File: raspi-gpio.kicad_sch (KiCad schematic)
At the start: 3 parts, among them J88 Conn_01x20_RPi_GPIO_Odd, J89 Conn_02x20_Odd_Even, J90 Conn_01x20_RPi_GPIO_Even

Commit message: Add JLCPCB corrections
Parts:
- J88: JLCPCB_CORRECTION (none) -> 0;24.13;270
- J89: JLCPCB_CORRECTION (none) -> 1.27;24.13;270; now in the parts list
- J90: JLCPCB_CORRECTION (none) -> 2.54;24.13;270
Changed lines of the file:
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@@
+			"AAAAAAAAAAAAAAAAAAAAAAAAAAAAAAAAAAAAAAAAAAAAAAAAAAAAAAAAAAAAAAAAAAAAAAAAAAAA"
+			"AAAAAAAAAAAAAAAAAAAAAAAAAAAAAAAAAAAAAAAAAAAAAAAAAAAAAAAAAAAAAAAAAAAAAAAAAAAA"
+			"AAAAAAAAAAAAAAAAAAAAAAAAAAAAAAAAAAAAAAAAAAAAAAAAAAAAAAAAAAAAAAAAAAAAAAAAAAAA"
+			"AAAAAAAAAAAAAAAAAAAAAAAAAAAAAAAAAAAAAAAAAAAAAAAAAAAAAAAAAAAAAAAAAAAAAAAAAAAA"
+			"AAAAAAAAAAAAAAAAAAAAAAAAAAAAAAAAAAAAAAAAAAAAAAAAAAAAAAAAAAAAAAAAAAAAAAAAAAAA"
+			"AAAAAAAAAAAAAAAAAAAAAAAAAAAAAAAAAAAAAAAAAAAAAAAAAAAAAAAAAAAAAAAAAAAAAAAAAAAA"
+			"AAAAAAAAAAAAAAAAAAAAAAAAAAAAAAAAAAAAAAAAAAAAAAAAAAAAAAAAAAAAAAAAAAAAAAAAAAAA"
+			"AAAAAAAAAAAAAAAAAAAAAAAAAAAAAAAAAAAAAAAAAAAAAAAAAAAAAAAAAAAAAAAAAAAAAAAAAAAA"
+			"AAAAAAAAAAAAAAAAAAAAAAAAAAAAAAAAAAAAAAAAAAAAAAAAAAAAAAAAAAAAAAAAAAAAAAAAAAAA"
+			"AAAAAAAAAAAAAAAAAAAAAAAAAAAAAAAAAAAAAAAAAAAAAAAAAAAAAAAAAAAAAAAAAAAAAAAAAAAA"
+			"AAAAAAAAAAAAAAAAAAAAAAAAAAAAAAAAAAAAAAAAAAAAAAAAAAAAAAAAAAAAAAAAAAAAAAAAAAAA"
+			"AAAAAAAAAAAAAAAAAAAAAAAAAAAAAAAAAAAAAAAAAAAAAAAAAAAAAAAAAAAAAAAAAAAAAAAAAAAA"
+			"AAAAAAAAAAAAAAAAAAAAAAAAAAAAAAAAAAAAAAAAAAAAAAAAAAAAAAAAAAAAAAAAAAAAAAAAAAAA"
+			"AAAAAAAAAAAAAAAAAAAAAAAAAAAAAAAAAAAAAAAAAAAAAAAAAAAAAAAAAAAAAAAAAAAAAAAAAAAA"
+			"AAAAAAAAAAAAAAAAAAAAAAAAAAAAAAAAAAAAAAAAAAAAAAAAAAAAAAAAAAAAAAAAAAAAAAAAAAAA"
+			"AAAAAAAAAAAAAAAAAAAAAAAAAAAAAAAAAAAAAAAAAAAAAAAAAAAAAAAAAAAAAAAAAAAAAAAAAAAA"
+			"AAAAAAAAAAAAAAAAAAAAAAAAAAAAAAAAAAAAAAAAAAAAAAAAAAAAAAAAAAAAAAAAAAAAAAAAAAAA"
+			"AAAAAAAAAAAAAAAAAAAAAAAAAAAAAAAAAAAAAAAAAAAAAAAAAAAAAAAAAAAAAAAAAAAAAAAAAAAA"
+			"AAAAAAAAAAAAAAAAAAAAAAAAAAAAAAAAAAAAAAAAAAAAAAAAAAAAAAAAAAAAAAAAAAAAAAAAAAAA"
+			"AAAAAAAAAAAAAAAAAAAAAAAAAAAAAAAAAAAAAAAAAAAAAAAAAAAAAAAAAAAAAAAAAAAAAAAAAAAA"
+			"AAAAAAAAAAAAAAAAAAAAAAAAAAAAAAAAAAAAAAAAAAAAAAAAAAAAAAAAAAAAAAAAAAAAAAAAAAAA"
+			"AAAAAAAAAAAAAAAAAAAAAAAAAAAAAAAAAAAAAAAAAAAAAAAAAAAAAAAAAAAAAAAAAAAAAAAAAAAA"
+			"AAAAAAAAAAAAAAAAAAAAAAAAAAAAAAAAAAAAAAAAAAAAAAAAAAAAAAAAAAAAAAAAAAAAAAAAAAAA"
+			"AAAAAAAAAAAAAAAAAAAAAAAAAAAAAAAAAAAAAAAAAAAAAAAAAAAAAAAAAAAAAAAAAAAAAAAAAAAA"
+			"AAAAAAAAAAAAAAAAAAAAAAAAAAAAAAAAAAAAAAAAAAAAAAAAAAAAAAAAAAAAAAAAAAAAAAAAAAAA"
+			"AAAAAAAAAAAAAAAAAAAAAAAAAAAAAAAAAAAAAAAAAAAAAAAAAAAAAAAAAAAAAAAAAAAAAAAAAAAA"
+			"AAAAAAAAAAAAAAAAAAAAAAAAAAAAAAAAAAAAAAAAAAAAAAAAAAAAAAAAAAAAAAAAAAAAAAAAAAAA"
+			"AAAAAAAAAAAAAAAAAAAAAAAAAAAAAAAAAAAAAAAAAAAAAAAAAAAAAAAAAAAAAAAAAAAAAAAAAAAA"
+			"AAAAAAAAAAAAAAAAAAAAAAAAAAAAAAAAAAAAAAAAAAAAAAAAAAAAAAAAAAAAAAAAAAAAAAAAAAAA"
+			"AAAAAAAAAAAAAAAAAAAAAAAAAAAAAAAAAAAAAAAAAAAAAAAAAAAAAAAAAAAAAAAAAAAAAAAAAAAA"
+			"AAAAAAAAAAAAAAAAAAAAAAAAAAAAAAAAAAAAAAAAAAAAAAAAAAAAAAAAAAAAAAAAAAAAAAAAAAAA"
+			"AAAAAAAAAAAAAAAAAAAAAAAAAAAAAAAAAAAAAAAAAAAAAAAAAAAAAAAAAAAAAAAAAAAAAAAAAAAA"
+			"AAAAAAAAAAAAAAAAAAAAAAAAAAAAAAAAAAAAAAAAAAAAAAAAAAAAAAAAAAAAAAAAAAAAAAAAAAAA"
+			"AAAAAAAAAAAAAAAAAAAAAAAAAAAAAAAAAAAAAAAAAAAAAAAAAAAAAAAAAAAAAAAAAAAAAAAAAAAA"
+			"AAAAAAAAAAAAAAAAAAAAAAAAAAAAAAAAAAAAAAAAAAAAAAAAAAAAAAAAAAAAAAAAAAAAAAAAAAAA"
+			"AAAAAAAAAAAAAAAAAAAAAAAAAAAAAAAAAAAAAAAAAAAAAAAAAAAAAAAAAAAAAAAAAAAAAAAAAAAA"
 			"AAAAAAAAAAAAAAAAAAAAAAAAAAAAAAAAAAAAAAAAAAAAAAAAAAAAAAAAAAAAAAAAAAAAAAAAAAAA"
 			"AAAAAAAAAAAAAAAAAAAAAAAAAAAAAAAAAAAAAAAAAAAAAAAAAAAAAAAAAAAAAAAAAAAAAAAAAAAA"
@@
 			)
 		)
+		(property "JLCPCB_CORRECTION" "0;24.13;270"
+			(at 119.38 83.82 0)
+			(effects
+				(font
+					(size 1.27 1.27)
+				)
+				(hide yes)
+			)
+		)
 		(pin "35"
 		)
@@
 		(unit 1)
 		(exclude_from_sim no)
-		(in_bom no)
+		(in_bom yes)
 		(on_board yes)
 		(dnp no)
@@
 		)
 		(property "THT_LCSC" ""
+			(at 142.24 83.82 0)
+			(effects
+				(font
+					(size 1.27 1.27)
+				)
+				(hide yes)
+			)
+		)
+		(property "JLCPCB_CORRECTION" "1.27;24.13;270"
 			(at 142.24 83.82 0)
 			(effects
@@
 			(at 167.64 83.82 0)
 			(effects
+				(font
+					(size 1.27 1.27)
+				)
+				(hide yes)
+			)
+		)
+		(property "JLCPCB_CORRECTION" "2.54;24.13;270"
+			(at 167.64 83.82 0)
+			(effects

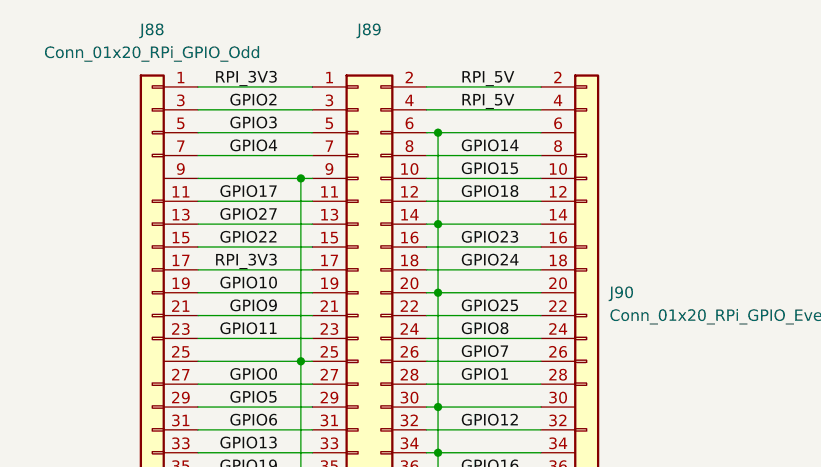
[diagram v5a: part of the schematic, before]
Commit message: Improve MCU2 layout; document curlim12v CSA
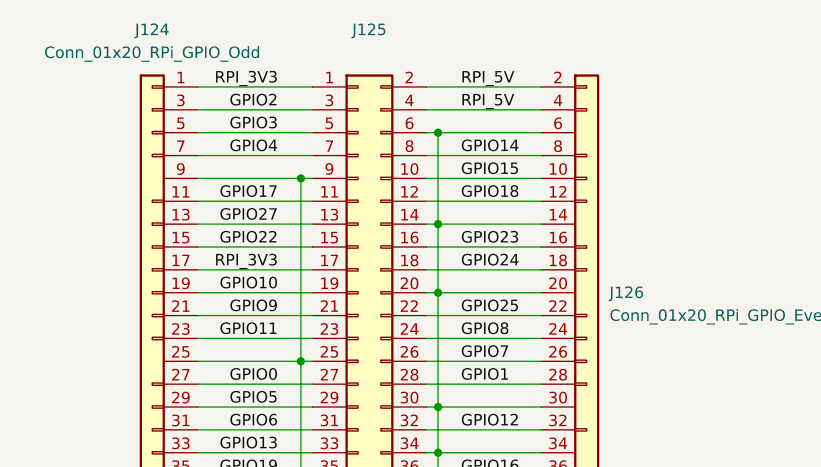
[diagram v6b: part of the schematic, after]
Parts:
- renumbered J88 to J124, J89 to J125, J90 to J126
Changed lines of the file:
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@@
 		(dnp no)
 		(fields_autoplaced yes)
-		(property "Reference" "J88"
+		(property "Reference" "J124"
 			(at 119.38 54.61 0)
 			(effects
@@
 			(project ""
 				(path "/7eeba806-440e-4671-bc07-69fe183910a7/d60c1020-d2cb-4d48-a4f2-2128439747bd"
-					(reference "J88")
+					(reference "J124")
 					(unit 1)
 				)
@@
 		(dnp no)
 		(fields_autoplaced yes)
-		(property "Reference" "J89"
+		(property "Reference" "J125"
 			(at 143.51 54.61 0)
 			(effects
@@
 			(project ""
 				(path "/7eeba806-440e-4671-bc07-69fe183910a7/d60c1020-d2cb-4d48-a4f2-2128439747bd"
-					(reference "J89")
+					(reference "J125")
 					(unit 1)
 				)
@@
 		(dnp no)
 		(fields_autoplaced yes)
-		(property "Reference" "J90"
+		(property "Reference" "J126"
 			(at 170.18 83.8199 0)
 			(effects
@@
 			(project ""
 				(path "/7eeba806-440e-4671-bc07-69fe183910a7/d60c1020-d2cb-4d48-a4f2-2128439747bd"
-					(reference "J90")
+					(reference "J126")
 					(unit 1)
 				)
@@
 		(dnp no)
 		(fields_autoplaced yes)
-		(property "Reference" "#PWR0270"
+		(property "Reference" "#PWR0271"
 			(at 135.89 118.11 0)
 			(effects
@@
 			(project ""
 				(path "/7eeba806-440e-4671-bc07-69fe183910a7/d60c1020-d2cb-4d48-a4f2-2128439747bd"
-					(reference "#PWR0270")
+					(reference "#PWR0271")
 					(unit 1)
 				)
@@
 		(dnp no)
 		(fields_autoplaced yes)
-		(property "Reference" "#PWR0271"
+		(property "Reference" "#PWR0272"
 			(at 151.13 118.11 0)
 			(effects
@@
 			(project "HALSPA"
 				(path "/7eeba806-440e-4671-bc07-69fe183910a7/d60c1020-d2cb-4d48-a4f2-2128439747bd"
-					(reference "#PWR0271")
+					(reference "#PWR0272")
 					(unit 1)
 				)

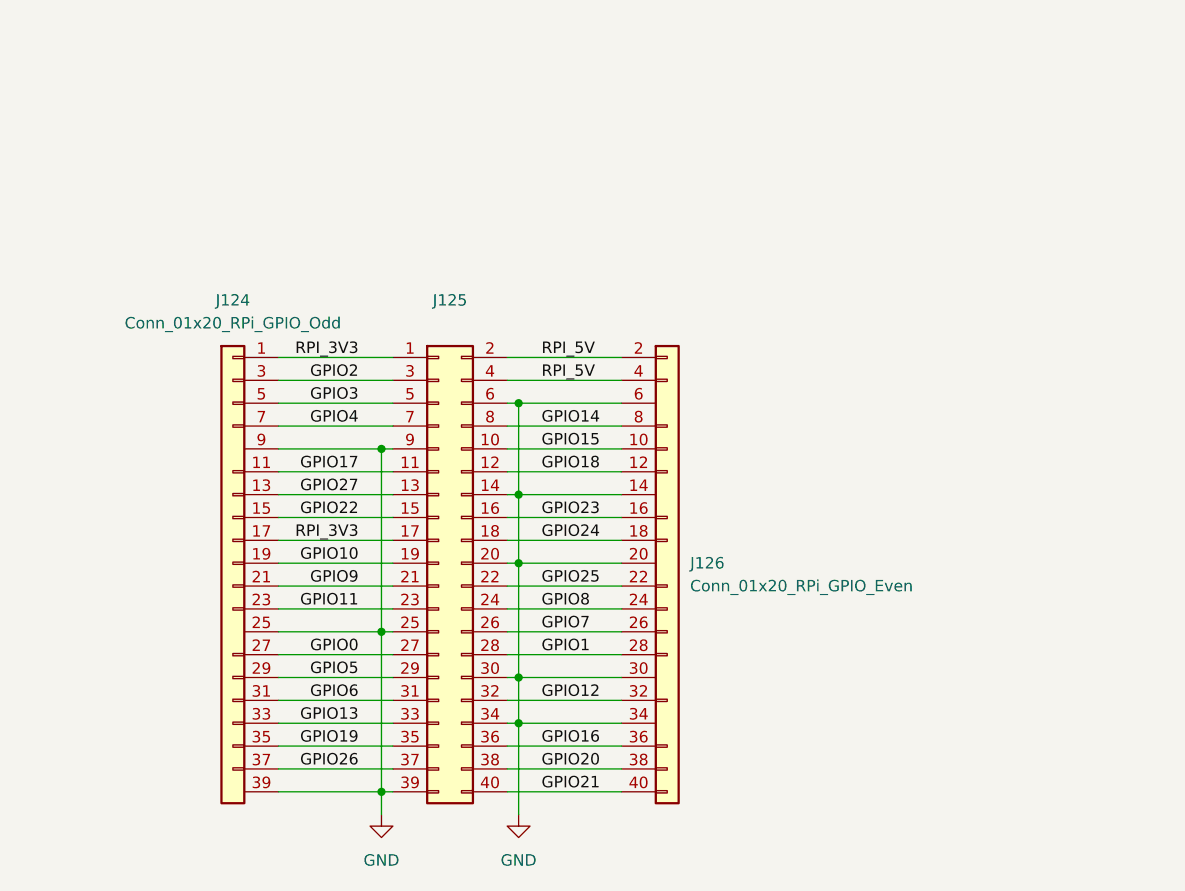
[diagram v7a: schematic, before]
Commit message: Update the design to a stackable one
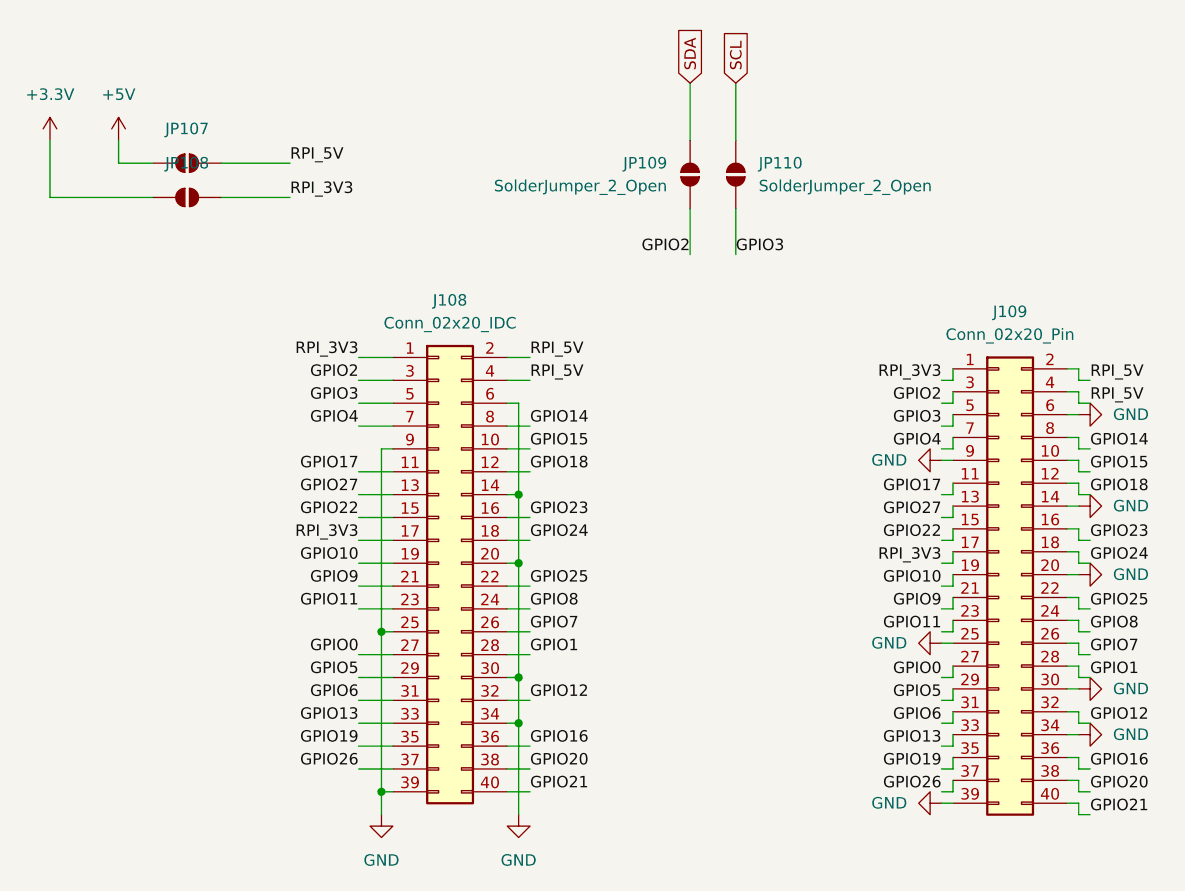
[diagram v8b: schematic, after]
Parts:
- removed J124: Conn_01x20_RPi_GPIO_Odd, HL_Connector_Pad_2.54mm:Pad_2x20_P2.54_1.7x1.7_RPi_GPIO_Odd, symbol HL_Connector_Pad_2.54mm:Conn_01x20_RPi_GPIO_Odd
- removed J126: Conn_01x20_RPi_GPIO_Even, HL_Connector_Pad_2.54mm:Pad_2x20_P2.54_1.7x1.7_RPi_GPIO_Even, symbol HL_Connector_Pad_2.54mm:Conn_01x20_RPi_GPIO_Even
- added J109: Conn_02x20_Pin, HL_Connector_Pad_2.54mm:Pad_2x20_P2.54_1.7x1.7_RPi-GPIO, symbol Connector_Generic:Conn_02x20_Odd_Even
- added JP107, JP108, JP109, JP110: SolderJumper_2_Open, Jumper:SolderJumper-2_P1.3mm_Open_TrianglePad1.0x1.5mm, symbol Jumper:SolderJumper_2_Open
- J108: renamed from J125; value Conn_02x20_Odd_Even -> Conn_02x20_IDC
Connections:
- net GND: now also J109.14 (Pin_14), J109.20 (Pin_20), J109.25 (Pin_25), J109.30 (Pin_30), J109.34 (Pin_34), J109.39 (Pin_39), J109.6 (Pin_6), J109.9 (Pin_9)
- net GPIO0: now also J109.27 (Pin_27)
- net GPIO1: now also J109.28 (Pin_28)
- net GPIO10: now also J109.19 (Pin_19)
- net GPIO11: now also J109.23 (Pin_23)
- net GPIO12: now also J109.32 (Pin_32)
- net GPIO13: now also J109.33 (Pin_33)
- net GPIO14: now also J109.8 (Pin_8)
- net GPIO15: now also J109.10 (Pin_10)
- net GPIO16: now also J109.36 (Pin_36)
- net GPIO17: now also J109.11 (Pin_11)
- net GPIO18: now also J109.12 (Pin_12)
- net GPIO19: now also J109.35 (Pin_35)
- net GPIO2: now also J109.3 (Pin_3), JP109.1 (A)
- net GPIO20: now also J109.38 (Pin_38)
- net GPIO21: now also J109.40 (Pin_40)
- net GPIO22: now also J109.15 (Pin_15)
- net GPIO23: now also J109.16 (Pin_16)
- net GPIO24: now also J109.18 (Pin_18)
- net GPIO25: now also J109.22 (Pin_22)
- net GPIO26: now also J109.37 (Pin_37)
- net GPIO27: now also J109.13 (Pin_13)
- net GPIO3: now also J109.5 (Pin_5), JP110.1 (A)
- net GPIO4: now also J109.7 (Pin_7)
- net GPIO5: now also J109.29 (Pin_29)
- net GPIO6: now also J109.31 (Pin_31)
- net GPIO7: now also J109.26 (Pin_26)
- net GPIO8: now also J109.24 (Pin_24)
- net GPIO9: now also J109.21 (Pin_21)
- net RPI_3V3: now also J109.1 (Pin_1), J109.17 (Pin_17), JP108.2 (B)
- net RPI_5V: now also J109.2 (Pin_2), J109.4 (Pin_4), JP107.2 (B)
- new net +3.3V: JP108.1 (A)
- new net +5V: JP107.1 (A)
- new net SCL: JP110.2 (B)
- new net SDA: JP109.2 (B)
